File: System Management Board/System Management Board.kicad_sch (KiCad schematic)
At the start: 129 parts, among them IC1 SI2318CDS-T1-GE3, IC2 SI2318CDS-T1-GE3, IC3 SI2318CDS-T1-GE3, IC4 SI2318CDS-T1-GE3, IC5 SI2318CDS-T1-GE3, IC6 SI2318CDS-T1-GE3, J1 Conn_01x04_Male, J10 Conn_01x02_Male, J11 Conn_02x20_Odd_Even, J12 Conn_02x05_Top_Bottom, J13 Conn_01x04_Female, J2 Conn_01x04_Male, J3 Conn_01x02_Male, J4 PJ-063BH, J5 Conn_01x02_Male, J6 Conn_02x06_Counter_Clockwise, J7 Conn_02x20_Odd_Even, J8 Conn_01x02_Male, J9 Conn_01x02_Male, K1 J115F11CH5VDCS61.5U, K2 J114FL1CS165VDC.41, K3 J114FL1CS165VDC.41, SW1 SW_Push, SW2 SW_Push, U1 SC0915, U2 OKI-78SR-5{slash}1.5-W36E-C, U3 OKI-78SR-5{slash}1.5-W36E-C, U4 AP7375-50W5-7, U5 74HC4051, U6 MCP9700T-ETT, U7 MCP9700T-ETT

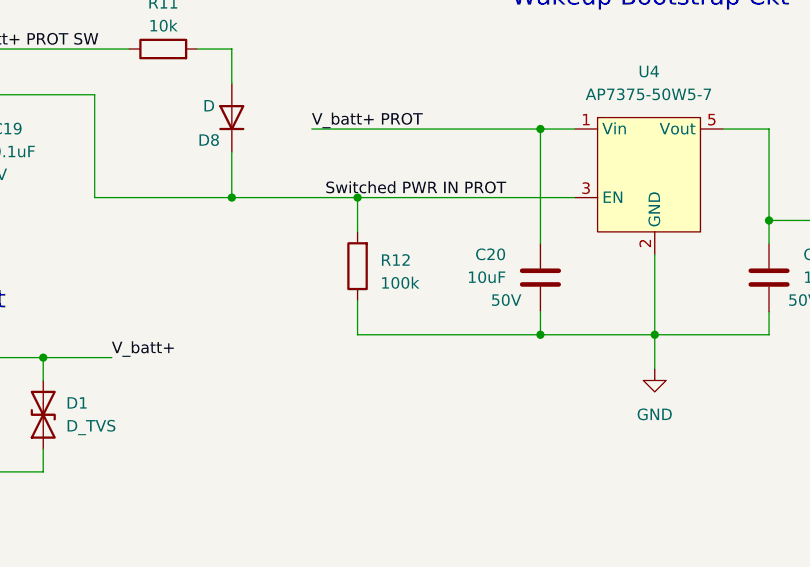
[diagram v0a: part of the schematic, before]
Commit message: Changed R12 from 100k to 10k
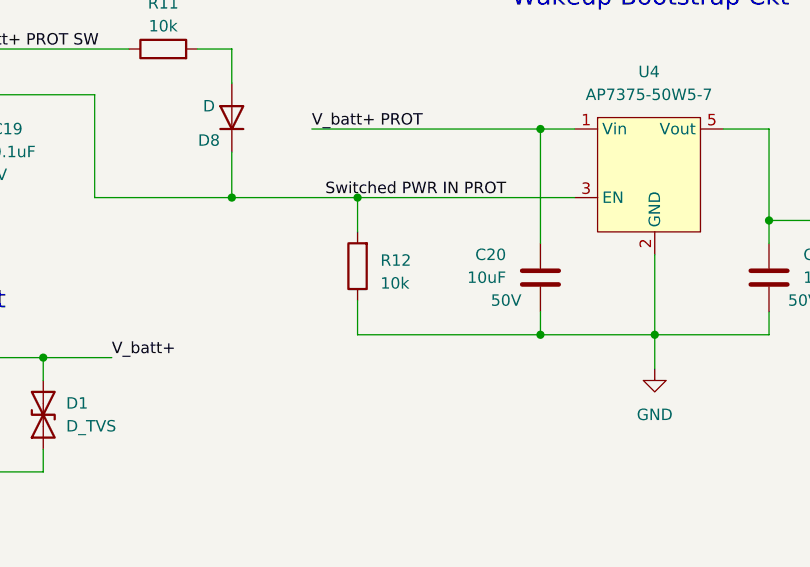
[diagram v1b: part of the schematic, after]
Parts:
- R12: value 100k -> 10k
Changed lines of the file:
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@@
       (effects (font (size 1.27 1.27)) (justify right))
     )
-    (property "Value" "100k" (at 134.62 50.165 0)
+    (property "Value" "10k" (at 134.62 50.165 0)
       (effects (font (size 1.27 1.27)) (justify right))
     )

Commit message: Added Bleeddown funtion to main sswithced power
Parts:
- added R40: 180, SMB:RES_3540_TEC, symbol Device:R
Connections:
- net 5V Relay PWR: now also K1.A1; no longer K1.A2
- net GND: now also R40.2
- net V_batt+ PROT: now also K1.14; no longer K1.11
- net V_batt+ PROT SW: now also K1.11; no longer K1.14
- net at D4.2 (A), IC1.3: now also K1.A2; no longer K1.A1
- net Cap Discharge: now reaches K1.12
- net Cap Discharge: now also R40.1
- no-connect marks 20 -> 19
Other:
- note added: "Must be high wattage res"
- moved on the sheet: D1, D10, D11, D12, D13, D16, D17, F10, H1, H2, H3, H4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

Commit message: Started adding thermal releifs and making pads larger, about 50% done
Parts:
- K2, K3: footprint Relay_THT:Relay_SPDT_Schrack-RT1-16A-FormC_RM5mm -> SMB:Big Pads - Relay_SPDT_Schrack-RT1-16A-FormC_RM5mm
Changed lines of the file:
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@@
       (effects (font (size 1.27 1.27)))
     )
-    (property "Footprint" "Relay_THT:Relay_SPDT_Schrack-RT1-16A-FormC_RM5mm" (at 501.65 66.04 0)
+    (property "Footprint" "SMB:Big Pads - Relay_SPDT_Schrack-RT1-16A-FormC_RM5mm" (at 501.65 66.04 0)
       (effects (font (size 1.27 1.27)) hide)
     )
@@
       (effects (font (size 1.27 1.27)))
     )
-    (property "Footprint" "Relay_THT:Relay_SPDT_Schrack-RT1-16A-FormC_RM5mm" (at 501.65 99.06 0)
-      (effects (font (size 1.27 1.27)) hide)
-    )
+    (property "Footprint" "SMB:Big Pads - Relay_SPDT_Schrack-RT1-16A-FormC_RM5mm" (at 501.65 99.06 0)
+      (effects (font (size 1.27 1.27)) hide)
+    )

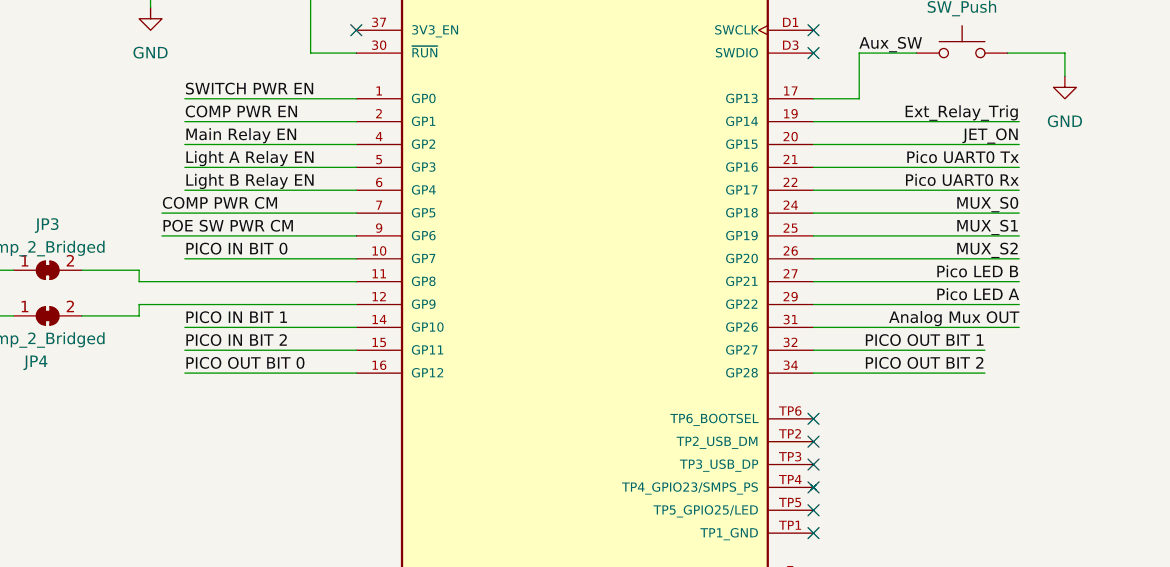
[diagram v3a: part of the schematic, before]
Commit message: Changed DC-DC current mesuremnt to anolog pin in schematic
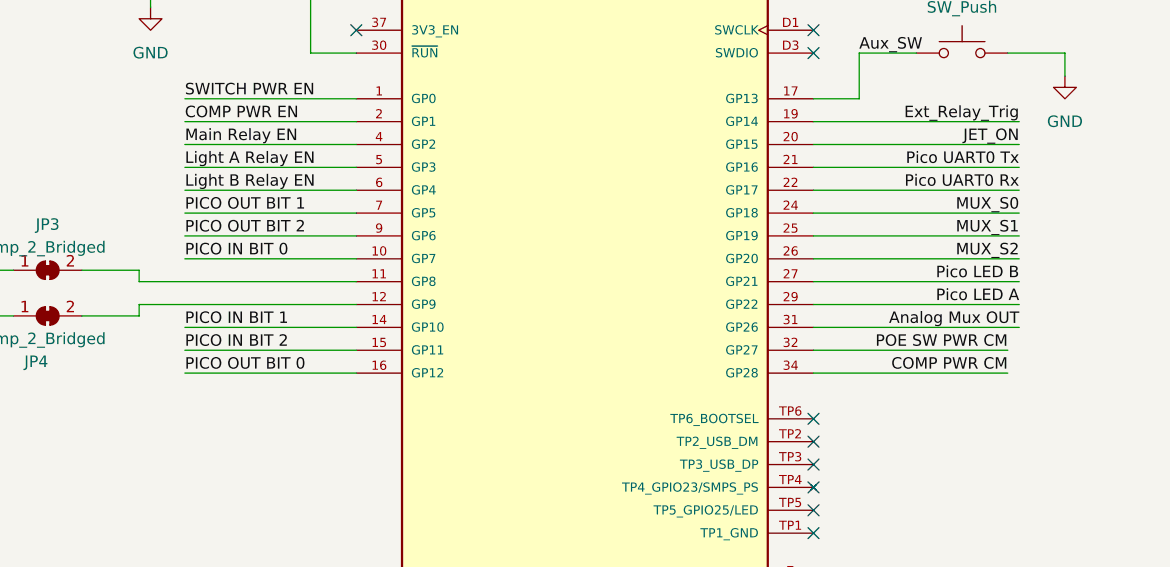
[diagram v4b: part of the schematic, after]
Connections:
- net COMP PWR CM: now also U1.34 (GP28); no longer U1.7 (GP5)
- net PICO OUT BIT 1: now also U1.7 (GP5); no longer U1.32 (GP27)
- net PICO OUT BIT 2: now also U1.9 (GP6); no longer U1.34 (GP28)
- net POE SW PWR CM: now also U1.32 (GP27); no longer U1.9 (GP6)
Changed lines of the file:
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@@
     (stroke (width 0) (type default))
   )
-  (wire (pts (xy 267.97 210.82) (xy 248.92 210.82))
+  (wire (pts (xy 179.07 195.58) (xy 198.12 195.58))
     (stroke (width 0) (type default))
   )
@@
     (stroke (width 0) (type default))
   )
-  (wire (pts (xy 267.97 213.36) (xy 248.92 213.36))
+  (wire (pts (xy 179.07 198.12) (xy 198.12 198.12))
     (stroke (width 0) (type default))
   )
@@
     (stroke (width 0) (type default))
   )
-  (wire (pts (xy 198.12 195.58) (xy 176.53 195.58))
+  (wire (pts (xy 248.92 213.36) (xy 270.51 213.36))
     (stroke (width 0) (type default))
   )
@@
     (stroke (width 0) (type default))
   )
-  (wire (pts (xy 198.12 198.12) (xy 176.53 198.12))
+  (wire (pts (xy 248.92 210.82) (xy 270.51 210.82))
     (stroke (width 0) (type default))
   )
@@
     (effects (font (size 1.27 1.27)) (justify left bottom))
   )
-  (label "PICO OUT BIT 2" (at 267.97 213.36 180) (fields_autoplaced)
-    (effects (font (size 1.27 1.27)) (justify right bottom))
+  (label "PICO OUT BIT 2" (at 179.07 198.12 0) (fields_autoplaced)
+    (effects (font (size 1.27 1.27)) (justify left bottom))
   )
   (label "POE_SW_Vout MES_ADC" (at 252.73 302.26 0) (fields_autoplaced)
@@
     (effects (font (size 1.27 1.27)) (justify left bottom))
   )
-  (label "PICO OUT BIT 1" (at 267.97 210.82 180) (fields_autoplaced)
-    (effects (font (size 1.27 1.27)) (justify right bottom))
+  (label "PICO OUT BIT 1" (at 179.07 195.58 0) (fields_autoplaced)
+    (effects (font (size 1.27 1.27)) (justify left bottom))
   )
   (label "JET_P26" (at 90.17 181.61 180) (fields_autoplaced)
@@
     (effects (font (size 1.27 1.27)) (justify left bottom))
   )
-  (label "POE SW PWR CM" (at 176.53 198.12 0) (fields_autoplaced)
-    (effects (font (size 1.27 1.27)) (justify left bottom))
+  (label "POE SW PWR CM" (at 270.51 210.82 180) (fields_autoplaced)
+    (effects (font (size 1.27 1.27)) (justify right bottom))
   )
   (label "PICO 3V3" (at 246.38 107.95 0) (fields_autoplaced)
@@
     (effects (font (size 1.27 1.27)) (justify left bottom))
   )
-  (label "COMP PWR CM" (at 176.53 195.58 0) (fields_autoplaced)
-    (effects (font (size 1.27 1.27)) (justify left bottom))
+  (label "COMP PWR CM" (at 270.51 213.36 180) (fields_autoplaced)
+    (effects (font (size 1.27 1.27)) (justify right bottom))
   )
   (label "5V Logic PWR" (at 279.4 33.02 0) (fields_autoplaced)

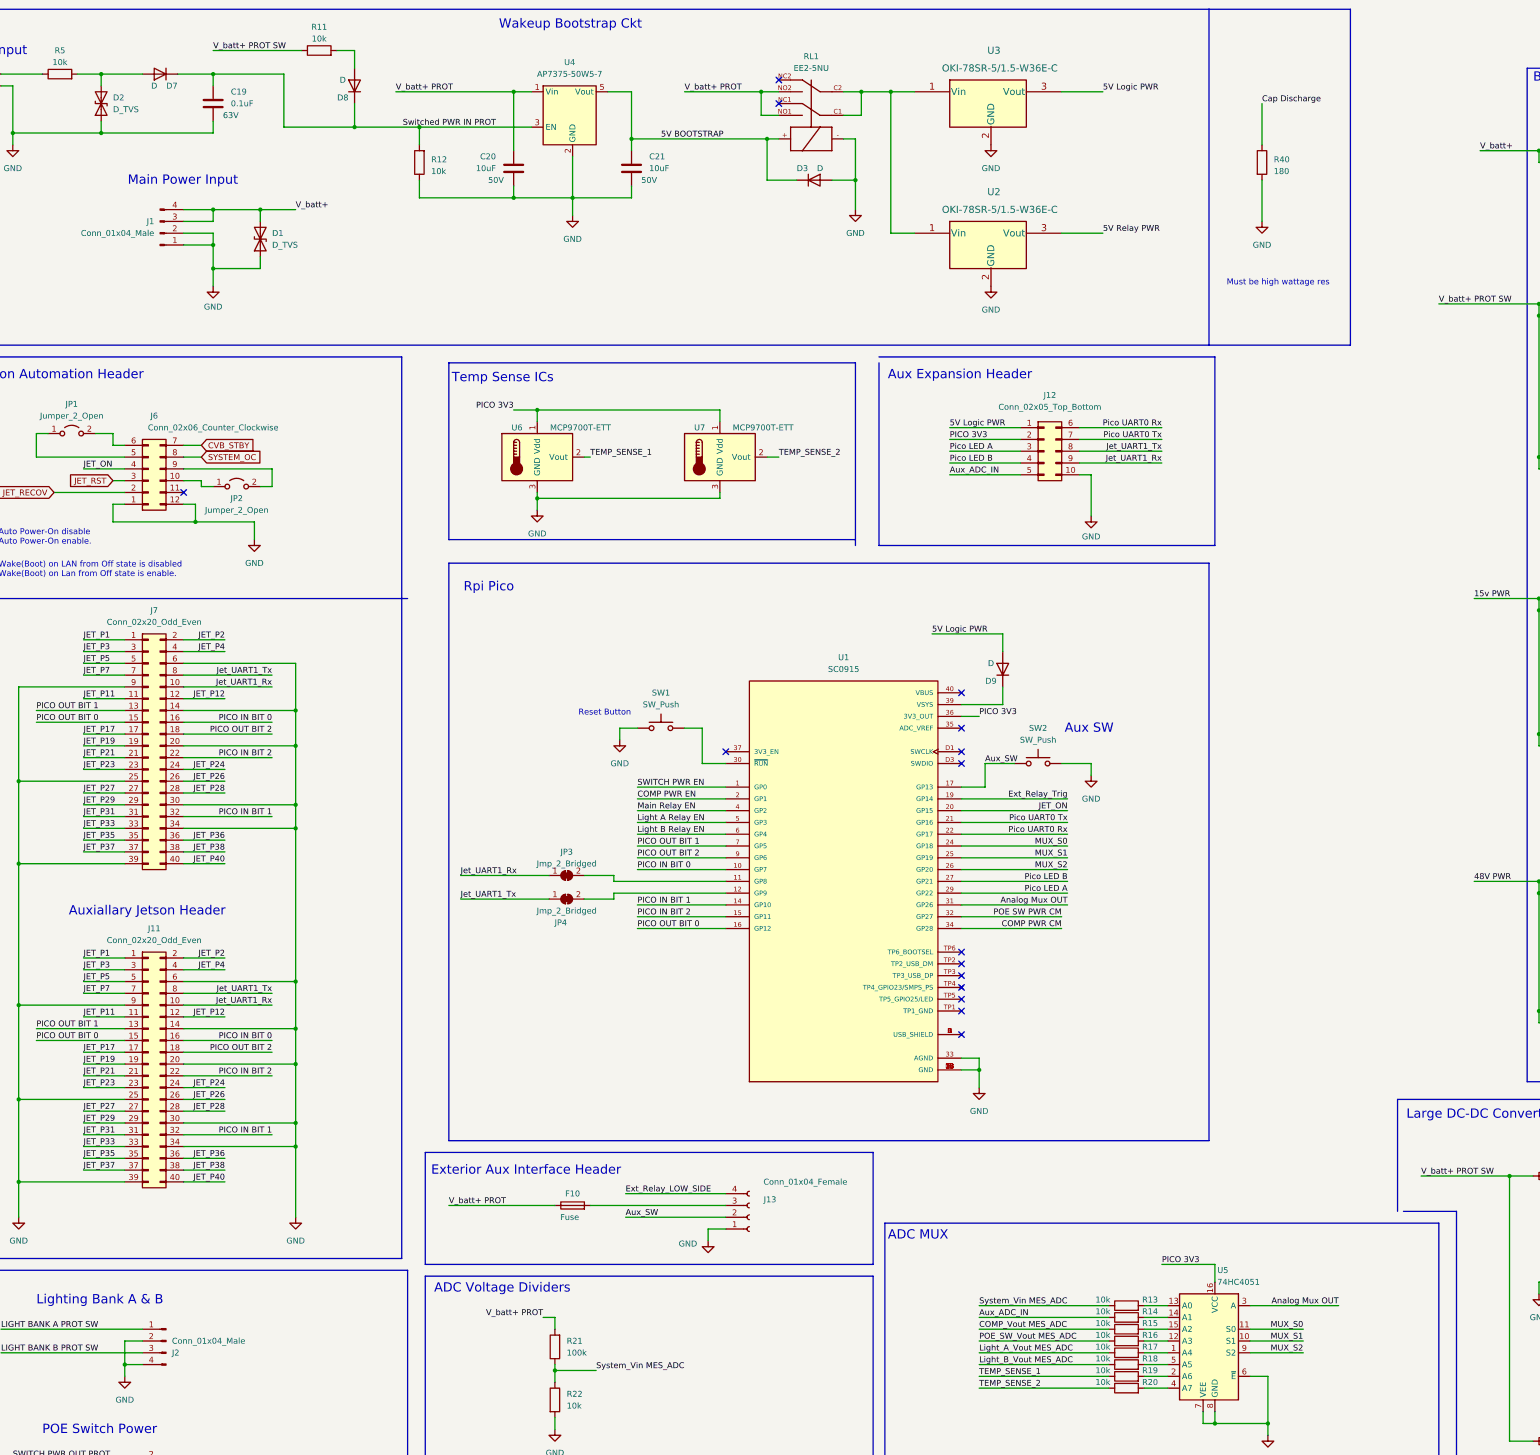
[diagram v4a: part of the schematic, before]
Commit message: Compleated refactoring schematic changes into Layout
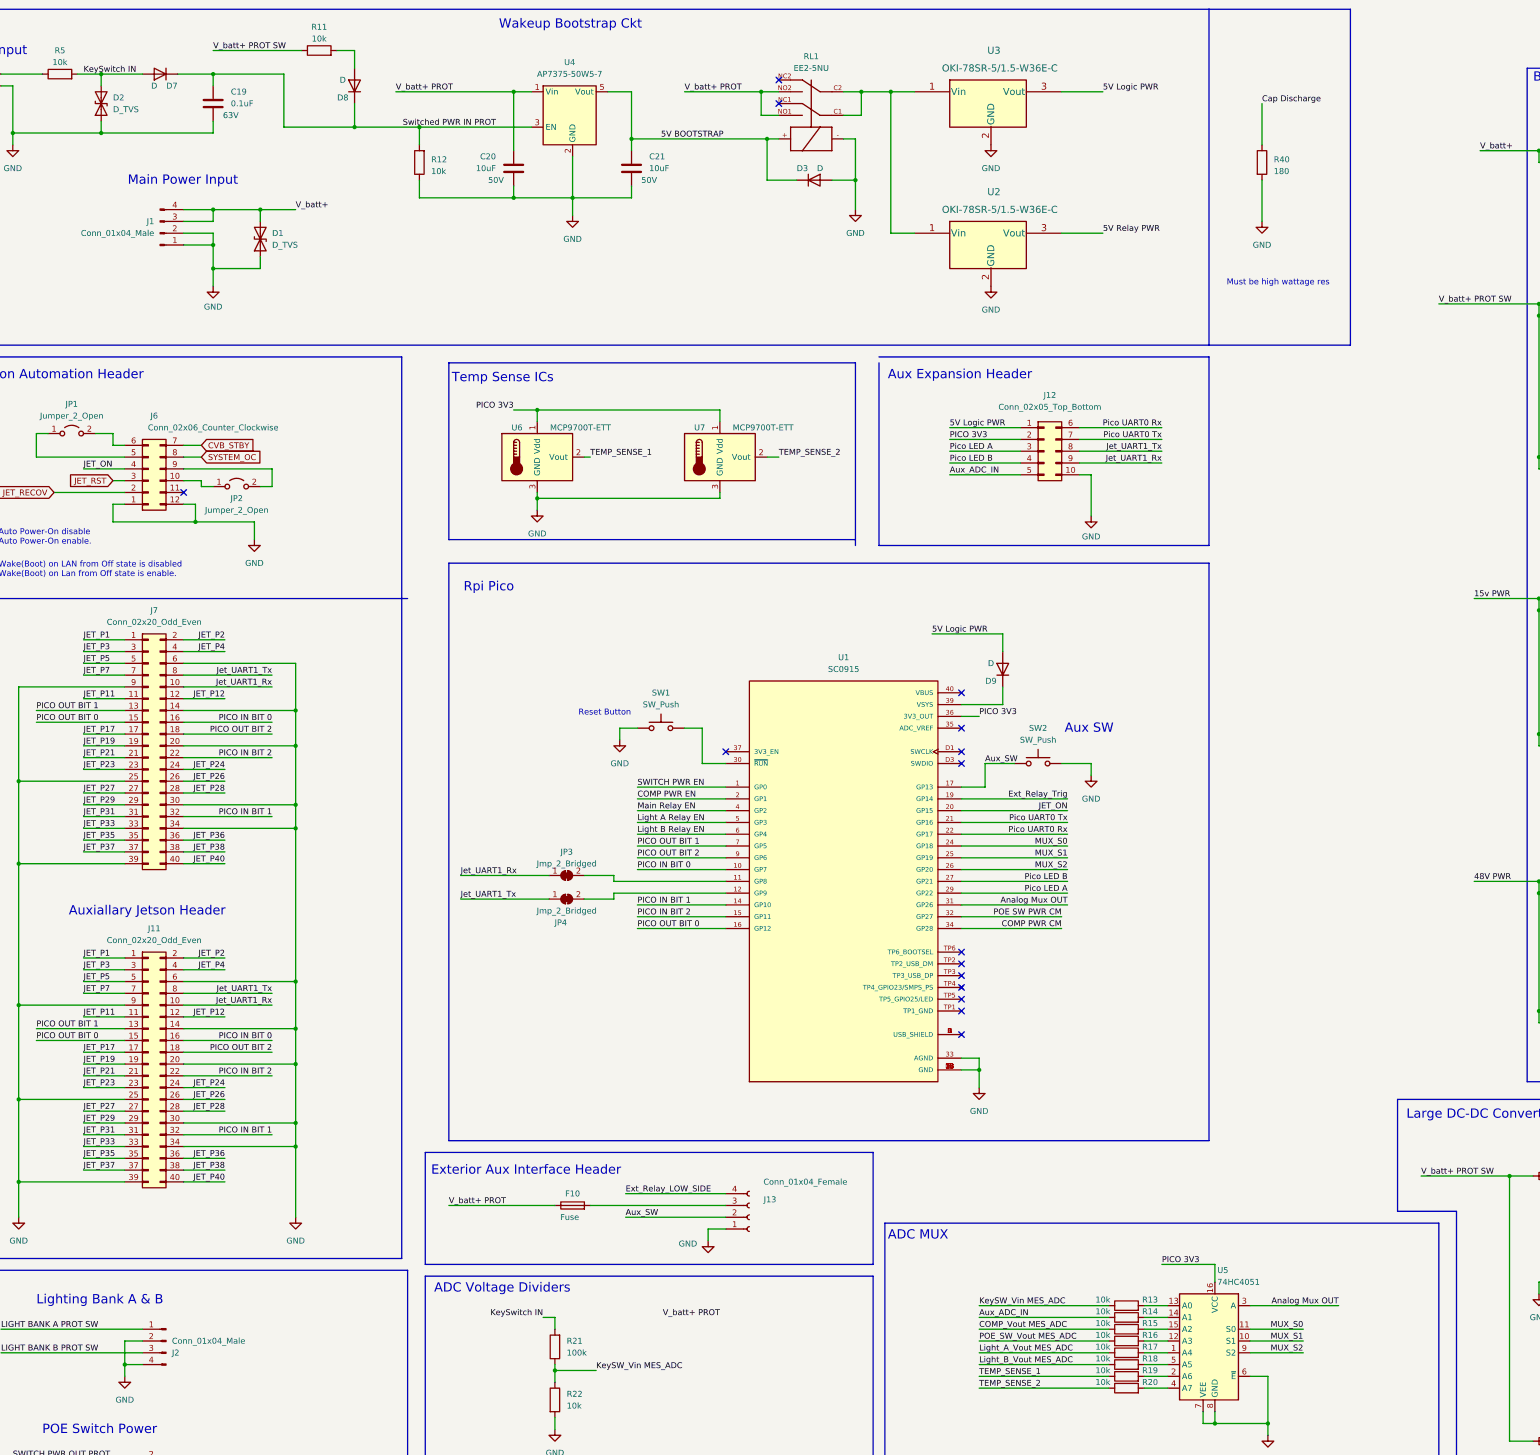
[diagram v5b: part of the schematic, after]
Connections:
- net V_batt+ PROT: no longer R21.2
- net KeySwitch IN: now reaches D2.2 (A2), D7.2 (A), R5.2
- net KeySwitch IN: now also R21.2
- net System_Vin MES_ADC renamed KeySW_Vin MES_ADC
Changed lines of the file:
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@@
     (stroke (width 0) (type default))
   )
-  (polyline (pts (xy 231.14 130.81) (xy 303.53 130.81))
+  (polyline (pts (xy 231.14 130.81) (xy 302.26 130.81))
     (stroke (width 0) (type default))
   )
@@
     (stroke (width 0) (type default))
   )
-  (polyline (pts (xy 303.53 130.81) (xy 303.53 90.17))
+  (polyline (pts (xy 302.26 130.81) (xy 302.26 90.17))
     (stroke (width 0) (type default))
   )
@@
     (stroke (width 0) (type default))
   )
-  (polyline (pts (xy 344.17 274.32) (xy 355.6 274.32))
+  (polyline (pts (xy 342.9 274.32) (xy 355.6 274.32))
     (stroke (width 0) (type default))
   )
@@
     (stroke (width 0) (type default))
   )
-  (polyline (pts (xy 231.14 90.17) (xy 303.53 90.17))
+  (polyline (pts (xy 231.14 90.17) (xy 302.26 90.17))
     (stroke (width 0) (type default))
   )
@@
     (effects (font (size 1.27 1.27)) (justify left bottom))
   )
+  (label "KeySW_Vin MES_ADC" (at 252.73 294.64 0) (fields_autoplaced)
+    (effects (font (size 1.27 1.27)) (justify left bottom))
+  )
   (label "COMP PWR EN" (at 524.51 144.78 0) (fields_autoplaced)
     (effects (font (size 1.27 1.27)) (justify left bottom))
@@
     (effects (font (size 1.27 1.27)) (justify left bottom))
   )
+  (label "KeySwitch IN" (at 158.75 297.18 180) (fields_autoplaced)
+    (effects (font (size 1.27 1.27)) (justify right bottom))
+  )
   (label "Light_A_Vout MES_ADC" (at 252.73 304.8 0) (fields_autoplaced)
     (effects (font (size 1.27 1.27)) (justify left bottom))
@@
     (effects (font (size 1.27 1.27)) (justify left bottom))
   )
-  (label "System_Vin MES_ADC" (at 252.73 294.64 0) (fields_autoplaced)
-    (effects (font (size 1.27 1.27)) (justify left bottom))
-  )
   (label "V_batt+" (at 360.68 45.72 0) (fields_autoplaced)
     (effects (font (size 1.27 1.27)) (justify left bottom))
@@
     (effects (font (size 1.27 1.27)) (justify right bottom))
   )
+  (label "KeySwitch IN" (at 59.69 29.21 0) (fields_autoplaced)
+    (effects (font (size 1.27 1.27)) (justify left bottom))
+  )
   (label "MUX_S2" (at 322.58 304.8 180) (fields_autoplaced)
     (effects (font (size 1.27 1.27)) (justify right bottom))
@@
     (effects (font (size 1.27 1.27)) (justify right bottom))
   )
-  (label "System_Vin MES_ADC" (at 170.18 308.61 0) (fields_autoplaced)
+  (label "KeySW_Vin MES_ADC" (at 170.18 308.61 0) (fields_autoplaced)
     (effects (font (size 1.27 1.27)) (justify left bottom))
   )
@@
     (effects (font (size 1.27 1.27)) (justify left bottom))
   )
-  (label "V_batt+ PROT" (at 158.75 297.18 180) (fields_autoplaced)
-    (effects (font (size 1.27 1.27)) (justify right bottom))
-  )
+  (label "V_batt+ PROT" (at 196.85 297.18 180) (fields_autoplaced)
+    (effects (font (size 1.27 1.27)) (justify right bottom))
+  )
